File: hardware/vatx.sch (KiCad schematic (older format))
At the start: 25 parts, among them J1 USB, P1 CONN_10X2, P3 CONN_1, P4 CONN_1, P5 CONN_1, P6 CONN_1, P7 CONN_1, SW1 SWITCH_INV, U1 LM317T

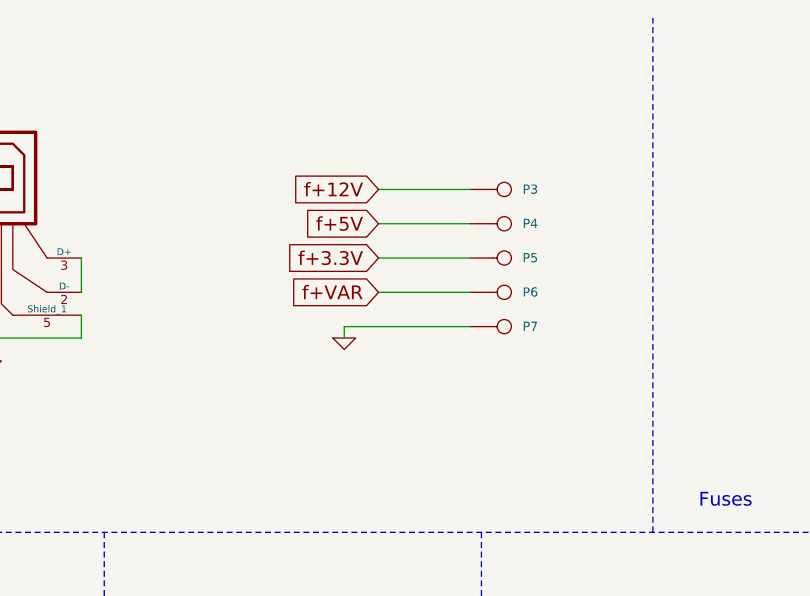
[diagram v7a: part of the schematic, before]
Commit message: Add pin-header for every voltage
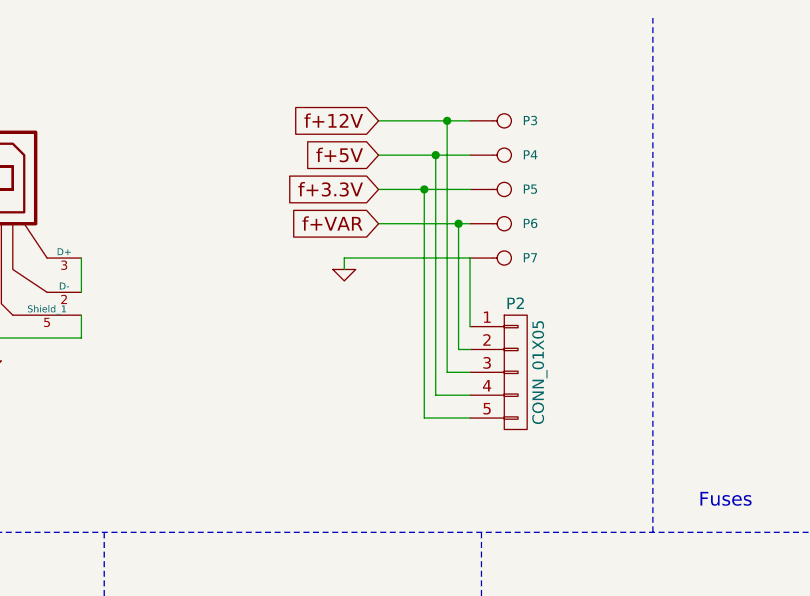
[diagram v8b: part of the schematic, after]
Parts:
- added P2: CONN_01X05, Pin_Headers:Pin_Header_Straight_1x05, symbol CONN_01X05
- D3, D4: footprint Diodes_SMD:Diode-MELF_Standard -> opl:DO-214AC
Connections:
- net GND: now also P2.1 (P1)
- net f+12V: now also P2.3 (P3)
- net f+3.3V: now also P2.5 (P5)
- net f+5V: now also P2.4 (P4)
- net f+VAR: now also P2.2 (P2)
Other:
- moved on the sheet: P3, P4, P5, P6, P7
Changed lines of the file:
@@
 +12V
 Wire Wire Line
-	6850 1250 7250 1250
+	6850 950  7250 950
 $Comp
 L CONN_1 P3
 U 1 1 5345D194
+P 7400 950
+F 0 "P3" H 7480 950 40  0000 L CNN
+F 1 "CONN_1" H 7400 1005 30  0001 C CNN
+F 2 "atx:Banana_single_6mmDrill" H 7400 950 60  0001 C CNN
+F 3 "" H 7400 950 60  0000 C CNN
+	1    7400 950
+	1    0    0    -1
+$EndComp
+Text GLabel 9200 1400 0    60   Input ~ 0
++5V
+Wire Wire Line
+	6850 1100 7250 1100
+$Comp
+L CONN_1 P4
+U 1 1 5345D1A4
+P 7400 1100
+F 0 "P4" H 7480 1100 40  0000 L CNN
+F 1 "CONN_1" H 7400 1155 30  0001 C CNN
+F 2 "atx:Banana_single_6mmDrill" H 7400 1100 60  0001 C CNN
+F 3 "" H 7400 1100 60  0000 C CNN
+	1    7400 1100
+	1    0    0    -1
+$EndComp
+Text GLabel 9200 1600 0    60   Input ~ 0
++3.3V
+Wire Wire Line
+	6850 1250 7250 1250
+$Comp
+L CONN_1 P5
+U 1 1 5345D1C1
 P 7400 1250
-F 0 "P3" H 7480 1250 40  0000 L CNN
+F 0 "P5" H 7480 1250 40  0000 L CNN
 F 1 "CONN_1" H 7400 1305 30  0001 C CNN
 F 2 "atx:Banana_single_6mmDrill" H 7400 1250 60  0001 C CNN
@@
 	1    0    0    -1
 $EndComp
-Text GLabel 9200 1400 0    60   Input ~ 0
-+5V
+Text GLabel 9200 1800 0    60   Input ~ 0
++VAR
 Wire Wire Line
 	6850 1400 7250 1400
 $Comp
-L CONN_1 P4
-U 1 1 5345D1A4
+L CONN_1 P6
+U 1 1 5345D1D1
 P 7400 1400
-F 0 "P4" H 7480 1400 40  0000 L CNN
+F 0 "P6" H 7480 1400 40  0000 L CNN
 F 1 "CONN_1" H 7400 1455 30  0001 C CNN
 F 2 "atx:Banana_single_6mmDrill" H 7400 1400 60  0001 C CNN
@@
 	1    0    0    -1
 $EndComp
-Text GLabel 9200 1600 0    60   Input ~ 0
-+3.3V
-Wire Wire Line
-	6850 1550 7250 1550
-$Comp
-L CONN_1 P5
-U 1 1 5345D1C1
+Wire Wire Line
+	6700 1550 7250 1550
+$Comp
+L CONN_1 P7
+U 1 1 5345D203
 P 7400 1550
-F 0 "P5" H 7480 1550 40  0000 L CNN
+F 0 "P7" H 7480 1550 40  0000 L CNN
 F 1 "CONN_1" H 7400 1605 30  0001 C CNN
 F 2 "atx:Banana_single_6mmDrill" H 7400 1550 60  0001 C CNN
@@
 	1    0    0    -1
 $EndComp
-Text GLabel 9200 1800 0    60   Input ~ 0
-+VAR
-Wire Wire Line
-	6850 1700 7250 1700
-$Comp
-L CONN_1 P6
-U 1 1 5345D1D1
-P 7400 1700
-F 0 "P6" H 7480 1700 40  0000 L CNN
-F 1 "CONN_1" H 7400 1755 30  0001 C CNN
-F 2 "atx:Banana_single_6mmDrill" H 7400 1700 60  0001 C CNN
-F 3 "" H 7400 1700 60  0000 C CNN
-	1    7400 1700
-	1    0    0    -1
-$EndComp
-Wire Wire Line
-	6700 1850 7250 1850
-$Comp
-L CONN_1 P7
-U 1 1 5345D203
-P 7400 1850
-F 0 "P7" H 7480 1850 40  0000 L CNN
-F 1 "CONN_1" H 7400 1905 30  0001 C CNN
-F 2 "atx:Banana_single_6mmDrill" H 7400 1850 60  0001 C CNN
-F 3 "" H 7400 1850 60  0000 C CNN
-	1    7400 1850
-	1    0    0    -1
-$EndComp
 $Comp
 L GND #PWR07
 U 1 1 5345D209
-P 6700 1900
-F 0 "#PWR07" H 6700 1900 30  0001 C CNN
-F 1 "GND" H 6700 1830 30  0001 C CNN
-F 2 "" H 6700 1900 60  0000 C CNN
-F 3 "" H 6700 1900 60  0000 C CNN
-	1    6700 1900
-	1    0    0    -1
-$EndComp
-Wire Wire Line
-	6700 1850 6700 1900
+P 6700 1600
+F 0 "#PWR07" H 6700 1600 30  0001 C CNN
+F 1 "GND" H 6700 1530 30  0001 C CNN
+F 2 "" H 6700 1600 60  0000 C CNN
+F 3 "" H 6700 1600 60  0000 C CNN
+	1    6700 1600
+	1    0    0    -1
+$EndComp
+Wire Wire Line
+	6700 1550 6700 1600
 Text GLabel 4700 1550 0    60   Input ~ 0
 f+5V
@@
 F 0 "D3" H 3850 3400 40  0000 C CNN
 F 1 "1N4007" H 3850 3200 40  0000 C CNN
-F 2 "Diodes_SMD:Diode-MELF_Standard" H 3850 3300 60  0001 C CNN
+F 2 "opl:DO-214AC" H 3850 3300 60  0001 C CNN
 F 3 "" H 3850 3300 60  0000 C CNN
 	1    3850 3300
@@
 F 0 "D4" H 4500 4000 40  0000 C CNN
 F 1 "1N4007" H 4500 3800 40  0000 C CNN
-F 2 "Diodes_SMD:Diode-MELF_Standard" H 4500 3900 60  0001 C CNN
+F 2 "opl:DO-214AC" H 4500 3900 60  0001 C CNN
 F 3 "" H 4500 3900 60  0000 C CNN
 	1    4500 3900
@@
 Text GLabel 9700 1800 2    60   Output ~ 0
 f+VAR
+Text GLabel 6850 950  0    60   Input ~ 0
+f+12V
+Text GLabel 6850 1100 0    60   Input ~ 0
+f+5V
 Text GLabel 6850 1250 0    60   Input ~ 0
-f+12V
+f+3.3V
 Text GLabel 6850 1400 0    60   Input ~ 0
-f+5V
-Text GLabel 6850 1550 0    60   Input ~ 0
-f+3.3V
-Text GLabel 6850 1700 0    60   Input ~ 0
 f+VAR
 Wire Notes Line
@@
 Wire Wire Line
 	4250 4150 4250 4650
+$Comp
+L CONN_01X05 P2
+U 1 1 5500BFE2
+P 7450 2050
+F 0 "P2" H 7450 2350 50  0000 C CNN
+F 1 "CONN_01X05" V 7550 2050 50  0000 C CNN
+F 2 "Pin_Headers:Pin_Header_Straight_1x05" H 7450 2050 60  0001 C CNN
+F 3 "" H 7450 2050 60  0000 C CNN
+	1    7450 2050
+	1    0    0    -1
+$EndComp
+Wire Wire Line
+	7250 1550 7250 1850
+Wire Wire Line
+	7250 1950 7200 1950
+Wire Wire Line
+	7200 1950 7200 1400
+Connection ~ 7200 1400
+Wire Wire Line
+	7250 2050 7150 2050
+Wire Wire Line
+	7250 2150 7100 2150
+Wire Wire Line
+	7250 2250 7050 2250
+Wire Wire Line
+	7150 2050 7150 950
+Connection ~ 7150 950
+Wire Wire Line
+	7100 2150 7100 1100
+Connection ~ 7100 1100
+Wire Wire Line
+	7050 2250 7050 1250
+Connection ~ 7050 1250
 $EndSCHEMATC
